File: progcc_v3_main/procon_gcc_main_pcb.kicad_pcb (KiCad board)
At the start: 4 copper layers, 110.9 x 59.5 mm, 105 parts, among them J1 Rumble, J2 Rumble, J3 To Button Board, J4 Conn_01x06_Female, J5 Conn_01x02_Pin, J9 USB_C_Receptacle, Q1 Q_PMOS_GDS, Q2 Q_PMOS_GDS, Q3 Q_PMOS_GDS, Q4 BSS138, Q5 BSS138, Q6 BSS138, SW1 GL18_SW, SW2 GL18_SW, SW3 TS-1187A-B-A-B, T1 36-8730, T2 36-8730, T3 36-8730, T4 36-8730, U1 GH39F (Hall SOT23), U10 MCP3002, U2 GH39F (Hall SOT23), U3 GH39F (Hall SOT23), U4 GH39F (Hall SOT23), U5 GL16112, U6 RP2040, U7 LP3986-33B3F, U8 MCP3002, U9 W25Q128JVS, Y1 Crystal_GND3

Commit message: Update button board
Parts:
- added SW4: ~, progcc_v3:TS35CA, F.Cu at (128.9, 101.5)
- moved TP7 0.93 mm to (133.0, 104.2)
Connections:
- J9 pad S1: unconnected-(J9-SHIELD-PadS1) -> GND
- U6 pad 17: unconnected-(U6-GPIO14-Pad17) -> MODE_BUTTON
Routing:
- net MODE_BUTTON: track 0.00 -> 30.4 mm, vias 0 -> 3
- net GND: track 104.6 -> 116.8 mm, vias 40 -> 41
- net N_DATA: track 52.7 -> 53.5 mm, vias 2 -> 3
- net +3V3: vias 30 -> 31

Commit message: Production files
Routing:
- added copper zone on B.Cu, net GND
- added copper zone on F.Cu, net GND
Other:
- rule pad_to_mask_clearance: 0.051 -> 0
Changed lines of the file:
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@@
       (dielectric_constraints no)
     )
-    (pad_to_mask_clearance 0.051)
-    (solder_mask_min_width 0.22)
+    (pad_to_mask_clearance 0)
     (allow_soldermask_bridges_in_footprints yes)
     (pcbplotparams
@@
       (drillshape 0)
       (scaleselection 1)
-      (outputdirectory "proboss/")
+      (outputdirectory "production/gerber/")
     )
   )
@@
     (fp_line (start 1.6 0.8) (end -1.6 0.8)
       (stroke (width 0.1) (type solid)) (layer "F.Fab"))
-    (pad "1" smd roundrect (at -1.4875 0 270) (size 1.425 1.75) (layers "F.Cu" "F.Paste" "F.Mask") (roundrect_rratio 0.175439)
+    (pad "1" smd roundrect (at -1.4875 0 270) (size 1.425 1.75) (layers "F.Cu" "F.Paste" "F.Mask") (roundrect_rratio 0.1754392982)
       (net 13 "+5V_PRE") (pintype "passive"))
-    (pad "2" smd roundrect (at 1.4875 0 270) (size 1.425 1.75) (layers "F.Cu" "F.Paste" "F.Mask") (roundrect_rratio 0.175439)
+    (pad "2" smd roundrect (at 1.4875 0 270) (size 1.425 1.75) (layers "F.Cu" "F.Paste" "F.Mask") (roundrect_rratio 0.1754392982)
       (net 3 "+5V") (pintype "passive"))
     (model "${KICAD6_3DMODEL_DIR}/Fuse.3dshapes/Fuse_1206_3216Metric.wrl"
@@
     (fp_line (start 3.5 3.5) (end -3.5 3.5)
       (stroke (width 0.1) (type solid)) (layer "F.Fab"))
-    (pad "" smd roundrect (at -0.8 -0.8 270) (size 1.29 1.29) (layers "F.Paste") (roundrect_rratio 0.193798))
-    (pad "" smd roundrect (at -0.8 0.8 270) (size 1.29 1.29) (layers "F.Paste") (roundrect_rratio 0.193798))
-    (pad "" smd roundrect (at 0.8 -0.8 270) (size 1.29 1.29) (layers "F.Paste") (roundrect_rratio 0.193798))
-    (pad "" smd roundrect (at 0.8 0.8 270) (size 1.29 1.29) (layers "F.Paste") (roundrect_rratio 0.193798))
+    (pad "" smd roundrect (at -0.8 -0.8 270) (size 1.29 1.29) (layers "F.Paste") (roundrect_rratio 0.1937976744))
+    (pad "" smd roundrect (at -0.8 0.8 270) (size 1.29 1.29) (layers "F.Paste") (roundrect_rratio 0.1937976744))
+    (pad "" smd roundrect (at 0.8 -0.8 270) (size 1.29 1.29) (layers "F.Paste") (roundrect_rratio 0.1937976744))
+    (pad "" smd roundrect (at 0.8 0.8 270) (size 1.29 1.29) (layers "F.Paste") (roundrect_rratio 0.1937976744))
     (pad "1" smd roundrect (at -3.4375 -2.6 270) (size 0.875 0.2) (layers "F.Cu" "F.Paste" "F.Mask") (roundrect_rratio 0.25)
       (net 1 "+3V3") (pinfunction "IOVDD") (pintype "power_in"))
@@
     (fp_line (start 1.6 0.8) (end -1.6 0.8)
       (stroke (width 0.1) (type solid)) (layer "F.Fab"))
-    (pad "1" smd roundrect (at -1.4875 0 90) (size 1.425 1.75) (layers "F.Cu" "F.Paste" "F.Mask") (roundrect_rratio 0.175439)
+    (pad "1" smd roundrect (at -1.4875 0 90) (size 1.425 1.75) (layers "F.Cu" "F.Paste" "F.Mask") (roundrect_rratio 0.1754392982)
       (net 11 "+3.3V_PRE") (pintype "passive"))
-    (pad "2" smd roundrect (at 1.4875 0 90) (size 1.425 1.75) (layers "F.Cu" "F.Paste" "F.Mask") (roundrect_rratio 0.175439)
+    (pad "2" smd roundrect (at 1.4875 0 90) (size 1.425 1.75) (layers "F.Cu" "F.Paste" "F.Mask") (roundrect_rratio 0.1754392982)
       (net 4 "Net-(D2-A)") (pintype "passive"))
     (model "${KICAD6_3DMODEL_DIR}/Fuse.3dshapes/Fuse_1206_3216Metric.wrl"
@@
     (fp_line (start 1.6 0.8) (end -1.6 0.8)
       (stroke (width 0.1) (type solid)) (layer "F.Fab"))
-    (pad "1" smd roundrect (at -1.4875 0) (size 1.425 1.75) (layers "F.Cu" "F.Paste" "F.Mask") (roundrect_rratio 0.175439)
+    (pad "1" smd roundrect (at -1.4875 0) (size 1.425 1.75) (layers "F.Cu" "F.Paste" "F.Mask") (roundrect_rratio 0.1754392982)
       (net 8 "RUMBLE-") (pintype "passive"))
-    (pad "2" smd roundrect (at 1.4875 0) (size 1.425 1.75) (layers "F.Cu" "F.Paste" "F.Mask") (roundrect_rratio 0.175439)
+    (pad "2" smd roundrect (at 1.4875 0) (size 1.425 1.75) (layers "F.Cu" "F.Paste" "F.Mask") (roundrect_rratio 0.1754392982)
       (net 7 "Net-(Q3-S)") (pintype "passive"))
     (model "${KICAD6_3DMODEL_DIR}/Fuse.3dshapes/Fuse_1206_3216Metric.wrl"
@@
     (fp_line (start 1.6 0.8) (end 1.6 -0.8)
       (stroke (width 0.1) (type solid)) (layer "F.Fab"))
-    (pad "1" smd roundrect (at -1.35 0 90) (size 1.4 1.35) (layers "F.Cu" "F.Paste" "F.Mask") (roundrect_rratio 0.185185)
+    (pad "1" smd roundrect (at -1.35 0 90) (size 1.4 1.35) (layers "F.Cu" "F.Paste" "F.Mask") (roundrect_rratio 0.1851851852)
       (net 4 "Net-(D2-A)") (pintype "passive"))
-    (pad "2" smd roundrect (at 1.35 0 90) (size 1.4 1.35) (layers "F.Cu" "F.Paste" "F.Mask") (roundrect_rratio 0.185185)
+    (pad "2" smd roundrect (at 1.35 0 90) (size 1.4 1.35) (layers "F.Cu" "F.Paste" "F.Mask") (roundrect_rratio 0.1851851852)
       (net 2 "GND") (pintype "passive"))
     (model "${KICAD6_3DMODEL_DIR}/Capacitor_Tantalum_SMD.3dshapes/CP_EIA-3216-18_Kemet-A.wrl"
@@
   (segment (start 131.959166 119.468777) (end 131.151347 120.276596) (width 0.15) (layer "B.Cu") (net 90))
   (segment (start 131.151347 120.276596) (end 126.910268 120.276596) (width 0.15) (layer "B.Cu") (net 90))
+  (zone (net 2) (net_name "GND") (layer "F.Cu") (hatch edge 0.5)
+    (priority 2)
+    (connect_pads (clearance 0.25))
+    (min_thickness 0.25) (filled_areas_thickness no)
+    (fill yes (thermal_gap 0.5) (thermal_bridge_width 0.5))
+    (polygon
+      (pts
+        (xy 66.802 84.328)
+        (xy 208.026 84.074)
+        (xy 208.534 159.766)
+        (xy 65.532 161.798)
+      )
+    )
+  )
   (zone (net 2) (net_name "GND") (layer "In1.Cu") (hatch edge 0.5)
     (priority 1)
@@
       )
     )
+  )
+  (zone (net 2) (net_name "GND") (layer "B.Cu") (hatch edge 0.5)
+    (priority 3)
+    (connect_pads (clearance 0.25))
+    (min_thickness 0.25) (filled_areas_thickness no)
+    (fill yes (thermal_gap 0.5) (thermal_bridge_width 0.5))
+    (polygon
+      (pts
+        (xy 65.278 81.788)
+        (xy 210.566 81.534)
+        (xy 211.074 161.29)
+        (xy 61.976 163.576)
+      )
+    )

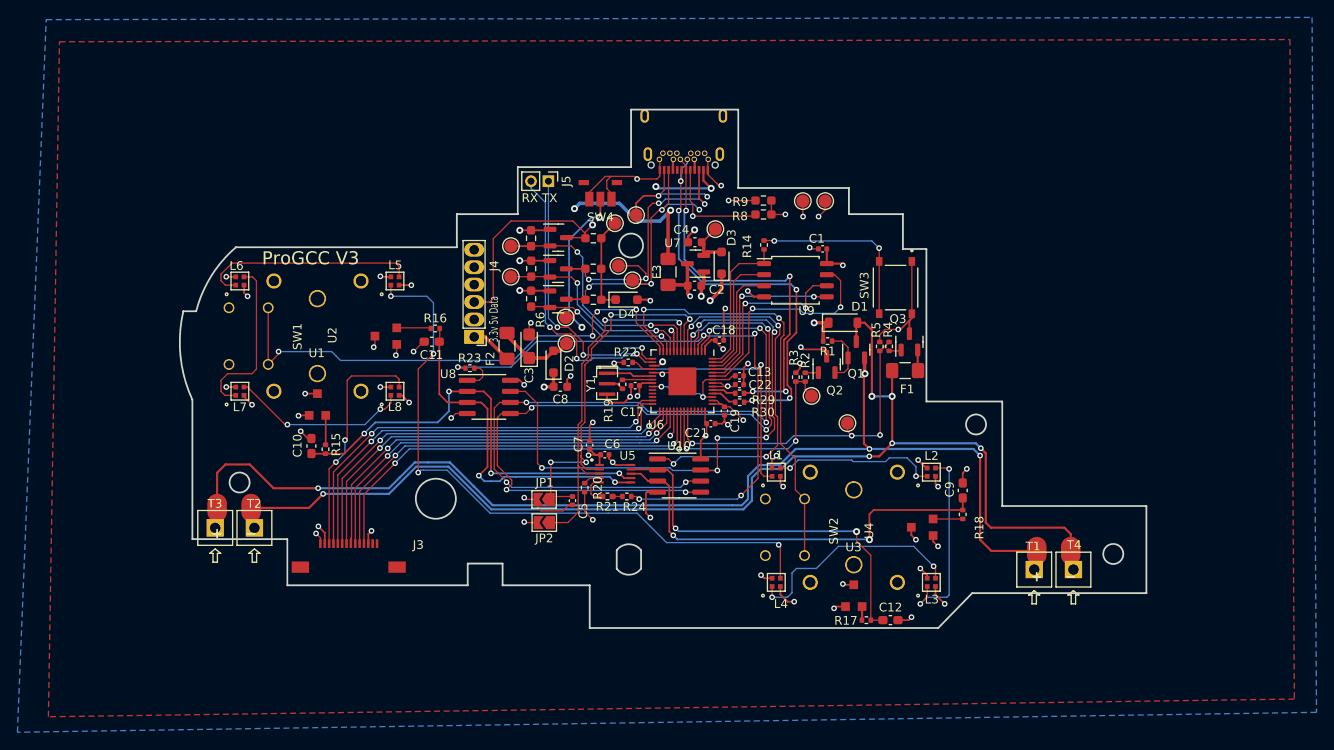
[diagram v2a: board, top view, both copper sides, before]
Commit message: Fixed missing trace
Missing trace and N Channel mosfet fix
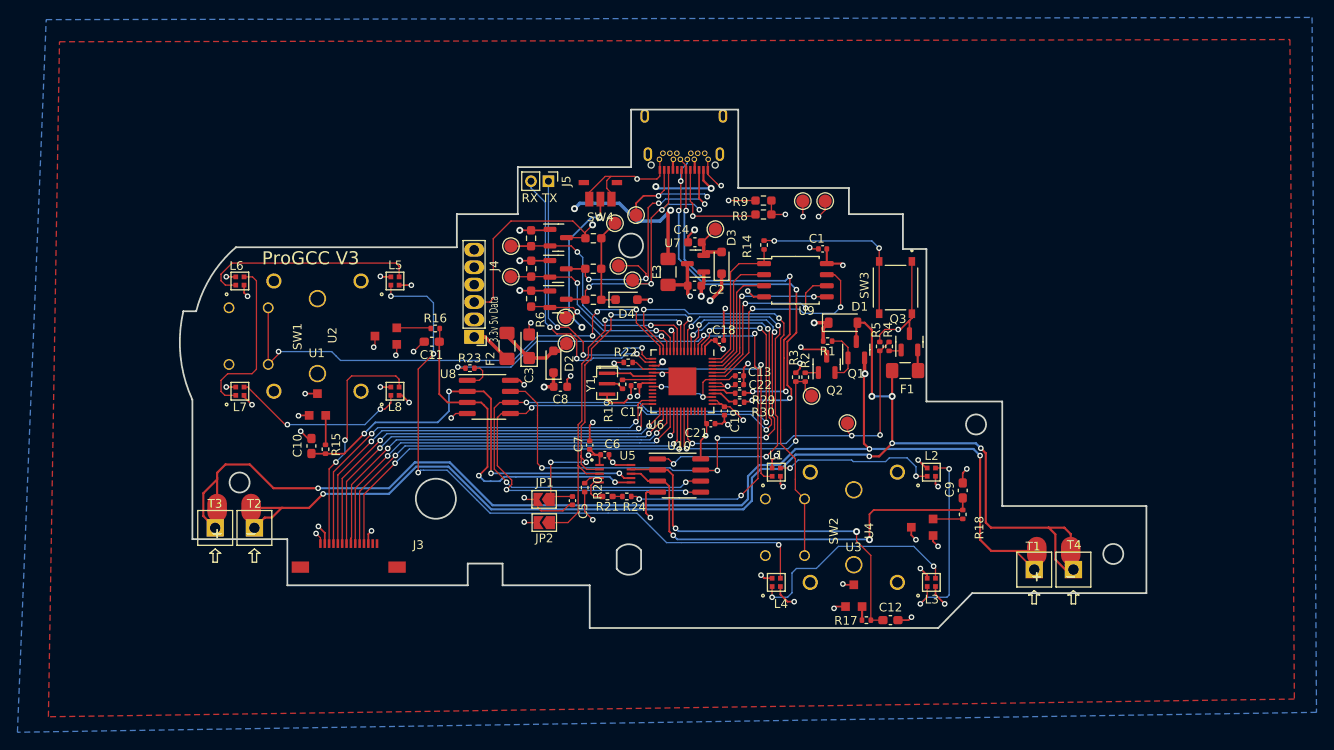
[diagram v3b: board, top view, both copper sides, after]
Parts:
- Q2, Q3: value Q_PMOS_GDS -> Q_NMOS_GSD
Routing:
- net RUMBLE-: track 143.3 -> 154.2 mm
- net +5V: track 186.8 -> 194.8 mm
- net N_CLOCK: track 41.3 -> 40.3 mm

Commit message: Update proto
- Update stick position
- Adjust some screw position slightly
- Fix schematic for Crystal and Rumble
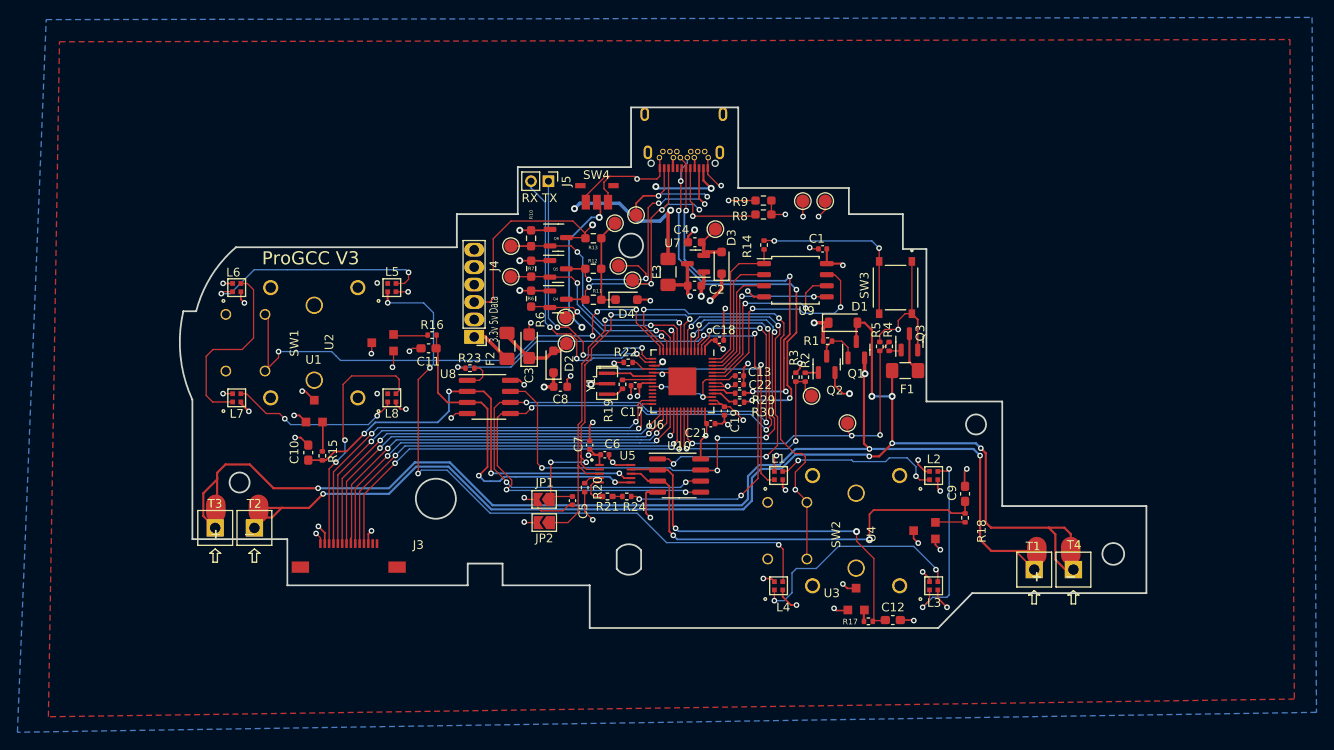
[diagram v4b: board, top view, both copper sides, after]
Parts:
- removed G***: LOGO, silks:natsu
- moved C11 0.84 mm to (109.2, 119.5)
- moved L5 0.84 mm to (104.9, 112.5)
- moved L6 0.84 mm to (87.1, 112.5)
- moved SW1 0.84 mm to (96.0, 118.9)
- moved U1 0.84 mm to (96.0, 118.9)
- moved U2 0.84 mm to (96.0, 118.9)
- moved L7 0.84 mm to (87.1, 125.2)
- moved L8 0.84 mm to (104.9, 125.2)
- moved R15 0.84 mm to (97.0, 131.9)
- moved C10 0.84 mm to (95.4, 131.5)
- moved R16 0.84 mm to (109.6, 118.0)
- moved SW4 0.53 mm to (128.5, 101.9)
- moved C9 0.47 mm to (170.7, 136.2)
- moved L1 0.47 mm to (149.3, 134.1)
- moved L2 0.47 mm to (167.1, 134.1)
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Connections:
- F1 pad 2: Net-(Q3-S) -> Net-(Q3-D)
- Q2 pad 2: Net-(Q1-G) -> GND
- Q2 pad 3: GND -> Net-(Q1-G)
- Q3 pad 2: Net-(Q3-S) -> GND
- Q3 pad 3: GND -> Net-(Q3-D)
- SW1 pad S1: LS_BUTTON -> SR_RGB
- SW1 pad S2: LS_BUTTON -> SR_RGB
- U6 pad 14: LS_BUTTON -> SR_RGB
- Y1 pad 2: Net-(R19-Pad1) -> GND
- Y1 pad 3: GND -> Net-(R19-Pad1)
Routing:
- net SR_RGB: track 75.6 -> 136.5 mm, vias 4 -> 8
- net LS_BUTTON: track 59.6 -> 0.00 mm, vias 4 -> 0
- net Net-(Q3-D): track 0.00 -> 4.65 mm
- net GND: track 116.8 -> 119.8 mm, vias 41 -> 42
- net Net-(Q3-S): track 2.38 -> 0.00 mm
- net RS_BUTTON: track 50.4 -> 52.4 mm, vias 2 -> 3
- net Net-(L6-DOUT): track 19.5 -> 21.4 mm
- net +3V3: track 82.1 -> 83.8 mm
- net Net-(L5-DOUT): track 25.0 -> 26.6 mm, vias 0 -> 2
- net BUTTON_RGB: track 26.8 -> 27.9 mm
- net Net-(Q1-G): track 6.25 -> 5.32 mm
- net Net-(L7-DOUT): track 20.5 -> 19.6 mm
- net LX: track 50.1 -> 50.8 mm
- net LY: track 40.2 -> 39.5 mm
- net RY: track 48.8 -> 49.3 mm
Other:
- board size 110.9 x 59.5 mm -> 110.9 x 59.7 mm

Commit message: Major updates
-Revised button board outline
-Added IMU for motion
-Cleaned up traces on main board
-Add test pads to button board
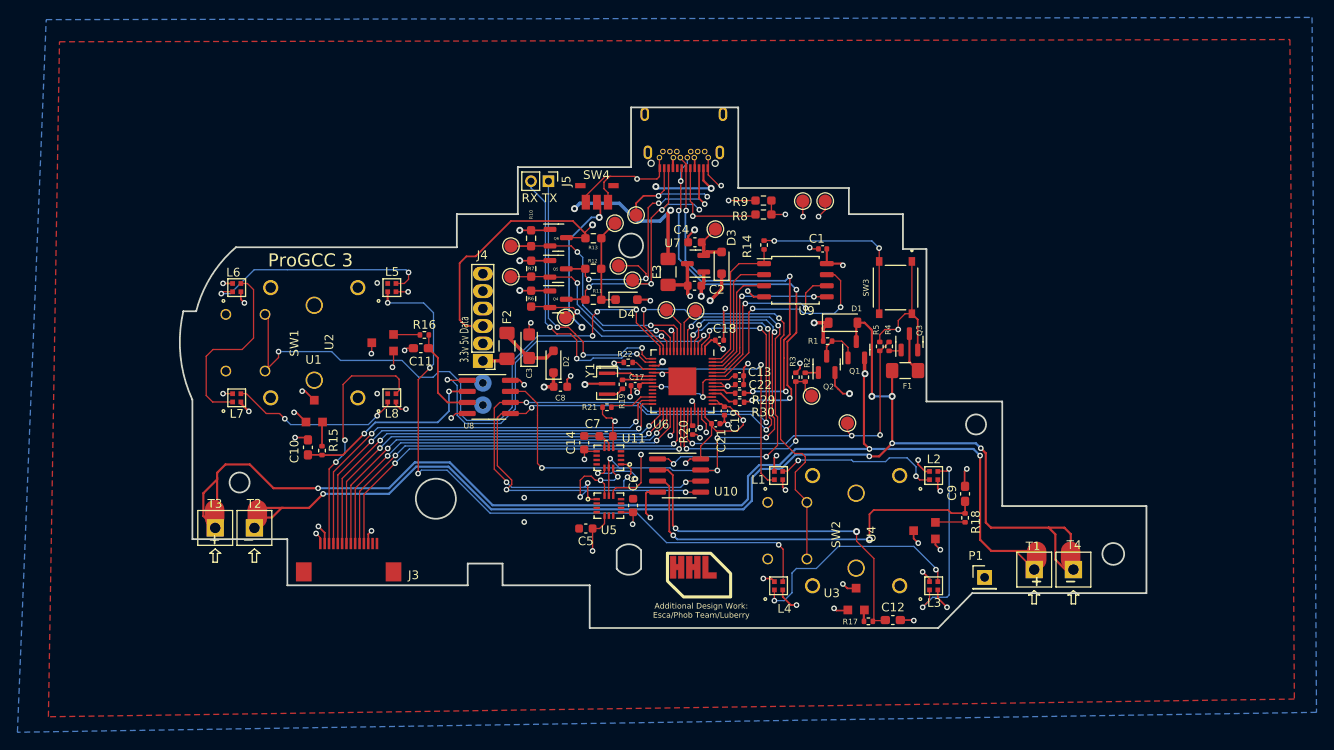
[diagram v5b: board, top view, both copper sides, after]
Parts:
- removed JP1, JP2: SolderJumper_2_Open, Jumper:SolderJumper-2_P1.3mm_Open_TrianglePad1.0x1.5mm
- removed R23, R24: 0, Resistor_SMD:R_0402_1005Metric
- added C14: 100nF, Capacitor_SMD:C_0603_1608Metric, F.Cu at (127.0, 130.3)
- added P1: Endpoint, Connector_PinHeader_2.54mm:PinHeader_1x01_P2.54mm_Vertical, F.Cu at (173.0, 145.8)
- added REF**: HHL_Logo, progcc_v3:HHL_Logo, F.Cu at (139.5, 146.0)
- added TP10: TestPoint, TestPoint:TestPoint_Pad_D1.5mm, B.Cu at (115.4, 123.5)
- added TP15: TestPoint, TestPoint:TestPoint_Pad_D1.5mm, F.Cu at (139.8, 115.2)
- added TP16: TestPoint, TestPoint:TestPoint_Pad_D1.5mm, F.Cu at (136.5, 115.1)
- added U11: ST_LSM6, progcc_v3:LGA14, F.Cu at (129.9, 132.1)
- C5, C6: value 4.7uF -> 100nF; footprint Capacitor_SMD:C_0402_1005Metric -> Capacitor_SMD:C_0603_1608Metric
- C7: value 0.1uF -> 100nF; footprint Capacitor_SMD:C_0402_1005Metric -> Capacitor_SMD:C_0603_1608Metric
- J3: footprint procon_gcc:molex_5051101492_14P -> progcc_v3:molex_5051101492_14P
- R20: value 0 -> 500K
- R21: value 33 -> 10k; footprint Resistor_SMD:R_0402_1005Metric_Pad0.72x0.64mm_HandSolder -> Resistor_SMD:R_0402_1005Metric
- TP12: moved to B.Cu
- U5: value GL16112 -> ST_LSM6; footprint progcc_v3:MSOP10 -> progcc_v3:LGA14
- moved R20 14.0 mm to (139.5, 128.9), turned to -90 degrees
- moved TP12 11.9 mm to (115.4, 126.0), turned to -90 degrees
- moved R21 10.2 mm to (129.6, 126.3), turned to 0 degrees
- moved C6 6.67 mm to (132.6, 137.6), turned to -90 degrees
- moved J3 4.58 mm to (100.0, 145.2)
- moved U5 3.74 mm to (129.9, 137.6), turned to 180 degrees
- moved C5 3.55 mm to (127.2, 140.2), turned to 0 degrees
- moved J4 2.93 mm to (115.4, 121.0)
- moved C7 2.15 mm to (129.5, 129.6), turned to 0 degrees
- moved C11 0.88 mm to (108.3, 119.5)
- moved R16 0.88 mm to (108.7, 118.0)
- moved J2 0.62 mm to (85.4, 138.5)
- moved C10 0.60 mm to (95.3, 130.9)
- moved R15 0.60 mm to (96.9, 131.3)
- moved C21 0.56 mm to (142.1, 128.2)
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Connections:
- net P_RCS renamed RADC_CS
- C5 pad 1: GULI_CALIBRATE -> GND
- C5 pad 2: GND -> +3V3
- C6 pad 1: +3V3 -> GND
- C6 pad 2: GND -> +3V3
- C7 pad 1: +3V3 -> GND
- C7 pad 2: GND -> +3V3
- R20 pad 1: +3V3 -> TOUCH_IN
- R20 pad 2: Net-(U5-PC2) -> TOUCH_OUT
- R21 pad 1: GULI_TXD -> +3V3
- R21 pad 2: Net-(U5-PC3) -> /RUN
- SW1 pad S1: SR_RGB -> LS_BUTTON
- SW1 pad S2: SR_RGB -> LS_BUTTON
- TP12 pad 1: Net-(D2-A) -> D+
- U10 pad 5: P_RX -> SPI_TX
- U10 pad 6: P_TX -> SPI_RX
- U10 pad 7: P_CLK -> SPI_CK
- U5 pad 1: +3V3 -> SPI_RX
- U5 pad 10: GND -> unconnected-(U5-NC-Pad10)
- U5 pad 2: GULI_CALIBRATE -> GND
- U5 pad 3: GULI_DZONE -> GND
- U5 pad 4: Net-(U5-PC2) -> unconnected-(U5-INT1-Pad4)
- U5 pad 5: Net-(U5-PC3) -> +3V3
- U5 pad 6: LY -> GND
- U5 pad 7: LX -> GND
- U5 pad 8: RY -> +3V3
- U5 pad 9: RX -> unconnected-(U5-INT2-Pad9)
- U6 pad 14: SR_RGB -> LS_BUTTON
- U6 pad 2: P_TX -> SPI_RX
- U6 pad 3: GPIO1 -> LADC_CS
- U6 pad 38: unconnected-(U6-GPIO26_ADC0-Pad38) -> TOUCH_IN
- U6 pad 39: unconnected-(U6-GPIO27_ADC1-Pad39) -> TOUCH_OUT
- U6 pad 4: P_CLK -> SPI_CK
- U6 pad 40: unconnected-(U6-GPIO28_ADC2-Pad40) -> IMU0_CS
- U6 pad 41: unconnected-(U6-GPIO29_ADC3-Pad41) -> IMU1_CS
- U6 pad 5: P_RX -> SPI_TX
- U6 pad 7: GULI_CALIBRATE -> GP1
- U6 pad 8: GULI_DZONE -> GP2
- U8 pad 1: P_LCS -> LADC_CS
- U8 pad 5: P_RX -> SPI_TX
- U8 pad 6: P_TX -> SPI_RX
- U8 pad 7: P_CLK -> SPI_CK
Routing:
- net SPI_TX: track 0.00 -> 98.8 mm, vias 0 -> 9
- net SPI_RX: track 0.00 -> 91.3 mm, vias 0 -> 8
- net P_RX: track 87.6 -> 0.00 mm, vias 6 -> 0
- net P_TX: track 84.1 -> 0.00 mm, vias 6 -> 0
- net SPI_CK: track 0.00 -> 74.7 mm, vias 0 -> 7
- net LS_BUTTON: track 0.00 -> 72.2 mm, vias 0 -> 4
- net GPIO1: track 71.2 -> 0.00 mm, vias 5 -> 0
- net P_CLK: track 68.6 -> 0.00 mm, vias 6 -> 0
- net SR_RGB: track 136.5 -> 75.7 mm, vias 8 -> 4
- net TOUCH_OUT: track 0.00 -> 57.6 mm, vias 0 -> 2
- net GULI_CALIBRATE: track 46.1 -> 0.00 mm, vias 4 -> 0
- net LADC_CS: track 0.00 -> 45.3 mm, vias 0 -> 2
- net GULI_DZONE: track 41.8 -> 0.00 mm, vias 2 -> 0
- net D+: track 43.8 -> 82.8 mm, vias 4 -> 5
- net D-: track 46.9 -> 84.0 mm, vias 5 -> 6
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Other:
- board text added: "5V"
- board text added: "Additional Design Work: Esca/Phob Team/Luberry"
- board text added: "D- D+"
- board text added: "GND"
- board text added: "ProGCC 3"
- board text removed: "ProGCC V3"
- board text removed: "d+"
- board text removed: "d-"
